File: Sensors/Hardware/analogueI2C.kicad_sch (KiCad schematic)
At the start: 136 parts, among them J10 1053131104, J11 1053131104, J12 1053131104, J13 1053131104, J14 1053131104, J3 1053131104, J4 1053131104, J5 1053131104, J6 1053131104, J7 1053131104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

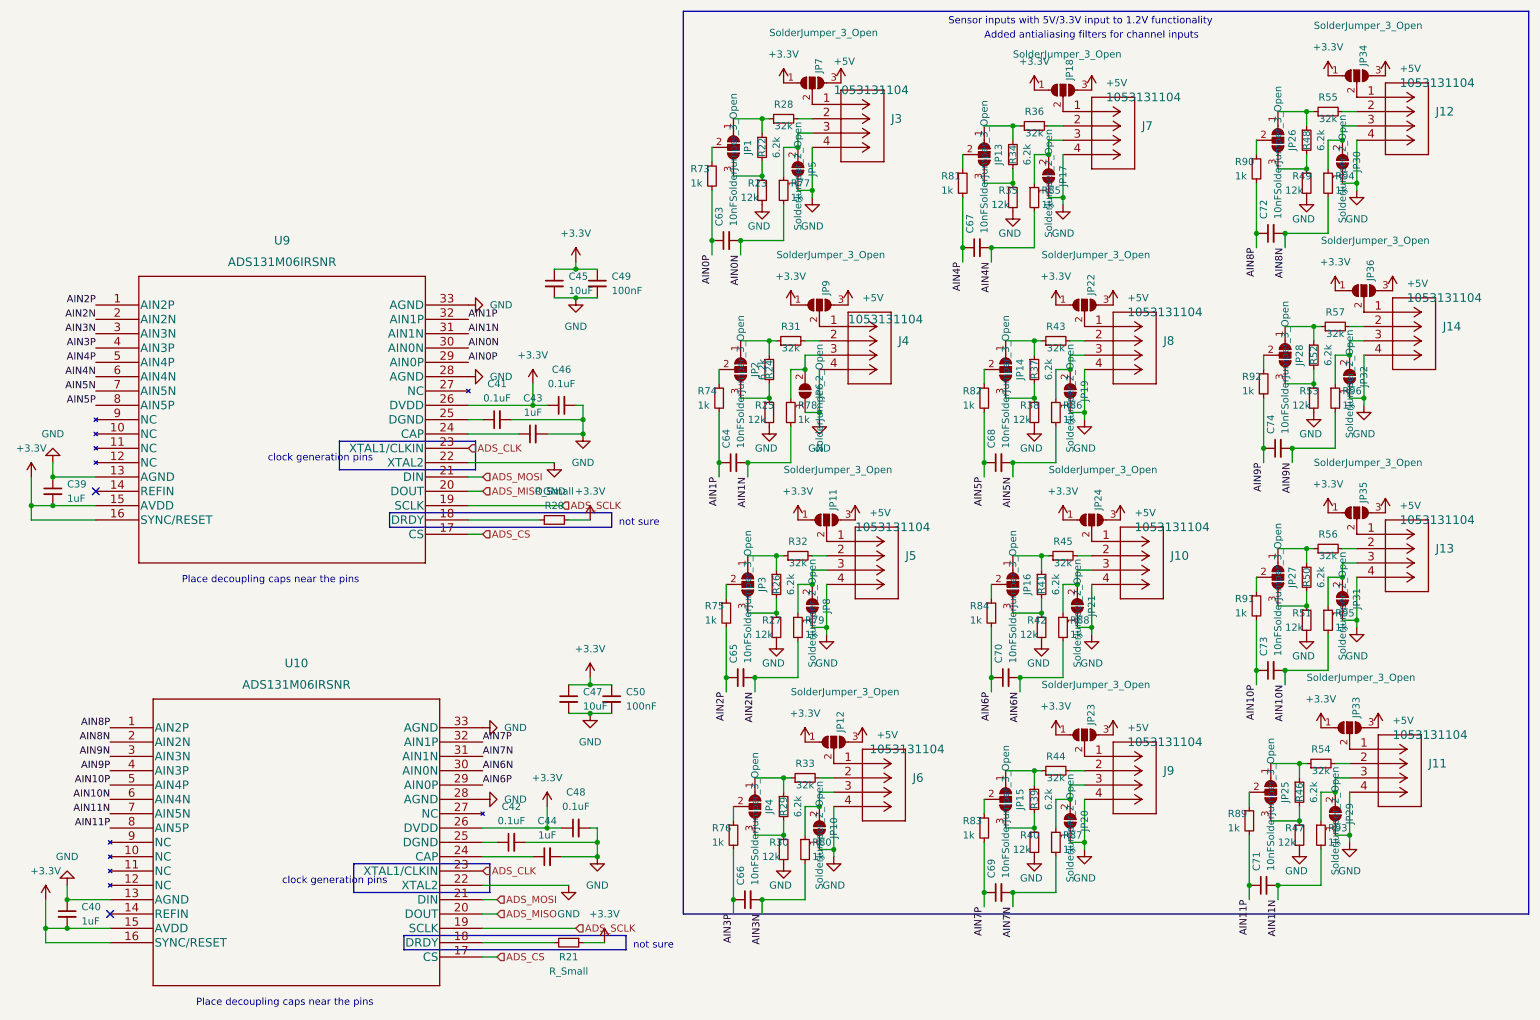
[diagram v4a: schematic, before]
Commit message: ADC connections and KiCAD version update
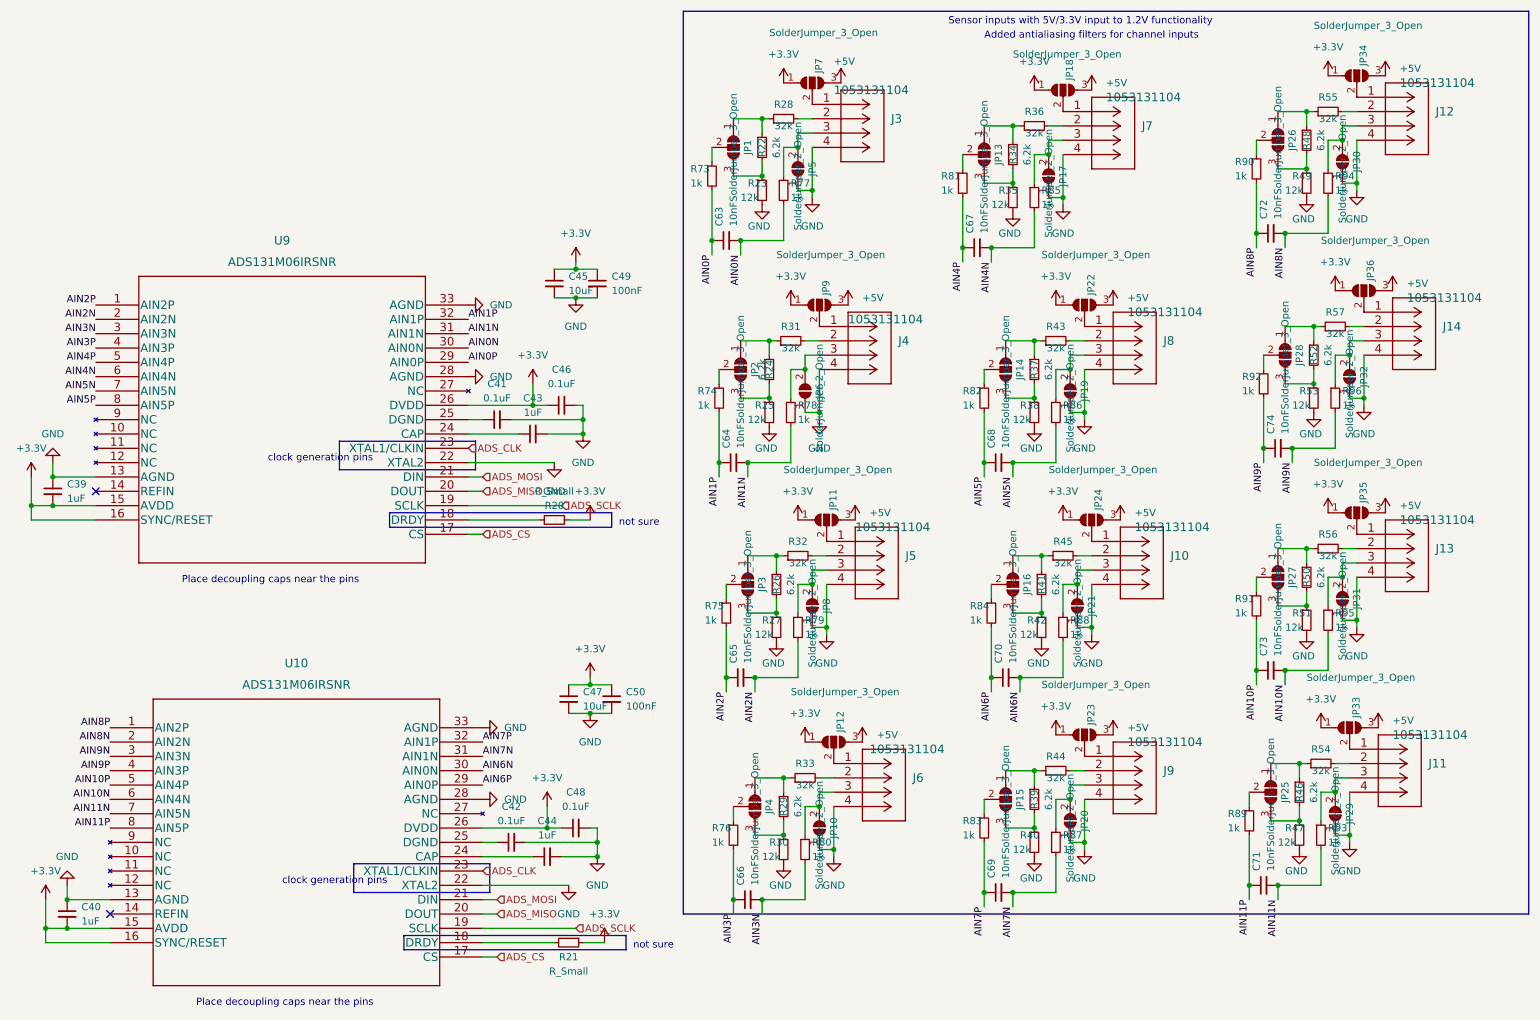
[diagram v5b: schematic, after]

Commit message: spacings and redo lines with tps
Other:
- note added: "10V option"
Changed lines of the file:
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@@
+    (effects (font (size 1.27 1.27)) (justify left bottom))
+  )
+  (text "10V option" (at 165.1 81.28 0)
     (effects (font (size 1.27 1.27)) (justify left bottom))
   )
@@
     (effects (font (size 1.27 1.27)) (justify left bottom))
   )
+  (text "10V option" (at 212.09 157.48 0)
+    (effects (font (size 1.27 1.27)) (justify left bottom))
+  )

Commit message: changed pins layout for esp
update for ADC traces
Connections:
- net +5V: no longer JP33.3 (B), JP35.3 (B)
- new net +10V: JP33.3 (B), JP35.3 (B)
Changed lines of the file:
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@@
     (effects (font (size 1.27 1.27)) (justify left bottom))
   )
-  (text "10V option" (at 165.1 81.28 0)
+  (text "10V option" (at 259.08 118.11 0)
     (effects (font (size 1.27 1.27)) (justify left bottom))
   )
@@
     (effects (font (size 1.27 1.27)) (justify left bottom))
   )
-  (text "10V option" (at 212.09 157.48 0)
+  (text "10V option" (at 257.81 157.48 0)
     (effects (font (size 1.27 1.27)) (justify left bottom))
   )
@@
     )
   )
-  (symbol (lib_id "power:+5V") (at 259.08 101.6 0) (unit 1)
-    (in_bom yes) (on_board yes) (dnp no) (fields_autoplaced)
-    (property "Reference" "#PWR0128" (at 259.08 105.41 0)
-      (effects (font (size 1.27 1.27)) hide)
-    )
-    (property "Value" "+5V" (at 261.62 100.3299 0)
-      (effects (font (size 1.27 1.27)) (justify left))
-    )
-    (property "Footprint" "" (at 259.08 101.6 0)
-      (effects (font (size 1.27 1.27)) hide)
-    )
-    (property "Datasheet" "" (at 259.08 101.6 0)
-      (effects (font (size 1.27 1.27)) hide)
-    )
-    (pin "1")
-    (instances
-      (project "sensorboard"
-        (path "/26801cfb-b53b-4a6a-a2f4-5f4986565765/00000000-0000-0000-0000-000061b9f0c0"
-          (reference "#PWR0128") (unit 1)
-        )
-      )
-    )
-  )
   (symbol (lib_id "Device:R_Small") (at 243.84 158.75 0) (unit 1)
     (in_bom yes) (on_board yes) (dnp no)
@@
     )
   )
+  (symbol (lib_id "power:+10V") (at 257.81 139.7 0) (unit 1)
+    (in_bom yes) (on_board yes) (dnp no) (fields_autoplaced)
+    (property "Reference" "#PWR023" (at 257.81 143.51 0)
+      (effects (font (size 1.27 1.27)) hide)
+    )
+    (property "Value" "+10V" (at 257.81 135.89 0)
+      (effects (font (size 1.27 1.27)))
+    )
+    (property "Footprint" "" (at 257.81 139.7 0)
+      (effects (font (size 1.27 1.27)) hide)
+    )
+    (property "Datasheet" "" (at 257.81 139.7 0)
+      (effects (font (size 1.27 1.27)) hide)
+    )
+    (pin "1")
+    (instances
+      (project "sensorboard"
+        (path "/26801cfb-b53b-4a6a-a2f4-5f4986565765/00000000-0000-0000-0000-000061b9f0c0"
+          (reference "#PWR023") (unit 1)
+        )
+      )
+    )
+  )
   (symbol (lib_id "Device:R_Small") (at 248.92 43.18 0) (unit 1)
     (in_bom yes) (on_board yes) (dnp no)
@@
     )
   )
+  (symbol (lib_id "power:+10V") (at 259.08 101.6 0) (unit 1)
+    (in_bom yes) (on_board yes) (dnp no) (fields_autoplaced)
+    (property "Reference" "#PWR022" (at 259.08 105.41 0)
+      (effects (font (size 1.27 1.27)) hide)
+    )
+    (property "Value" "+10V" (at 259.08 97.79 0)
+      (effects (font (size 1.27 1.27)))
+    )
+    (property "Footprint" "" (at 259.08 101.6 0)
+      (effects (font (size 1.27 1.27)) hide)
+    )
+    (property "Datasheet" "" (at 259.08 101.6 0)
+      (effects (font (size 1.27 1.27)) hide)
+    )
+    (pin "1")
+    (instances
+      (project "sensorboard"
+        (path "/26801cfb-b53b-4a6a-a2f4-5f4986565765/00000000-0000-0000-0000-000061b9f0c0"
+          (reference "#PWR022") (unit 1)
+        )
+      )
+    )
+  )
   (symbol (lib_id "Jumper:SolderJumper_3_Open") (at 207.01 102.87 0) (unit 1)
     (in_bom yes) (on_board yes) (dnp no)
@@
         )
       )
-    )
-  )
-  (symbol (lib_id "power:+5V") (at 257.81 139.7 0) (unit 1)
-    (in_bom yes) (on_board yes) (dnp no) (fields_autoplaced)
-    (property "Reference" "#PWR0126" (at 257.81 143.51 0)
-      (effects (font (size 1.27 1.27)) hide)
-    )
-    (property "Value" "+5V" (at 260.35 138.4299 0)
-      (effects (font (size 1.27 1.27)) (justify left))
-    )
-    (property "Footprint" "" (at 257.81 139.7 0)
-      (effects (font (size 1.27 1.27)) hide)
-    )
-    (property "Datasheet" "" (at 257.81 139.7 0)
-      (effects (font (size 1.27 1.27)) hide)
-    )
-    (pin "1")
-    (instances
-      (project "sensorboard"
-        (path "/26801cfb-b53b-4a6a-a2f4-5f4986565765/00000000-0000-0000-0000-000061b9f0c0"
-          (reference "#PWR0126") (unit 1)
-        )
-      )

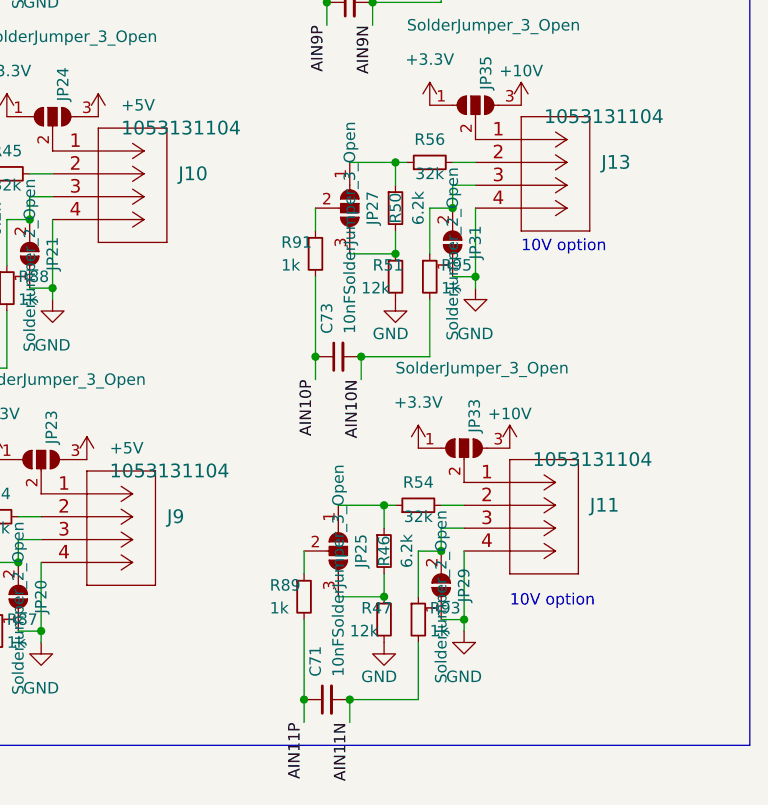
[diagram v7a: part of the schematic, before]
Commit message: added values for the 10V option
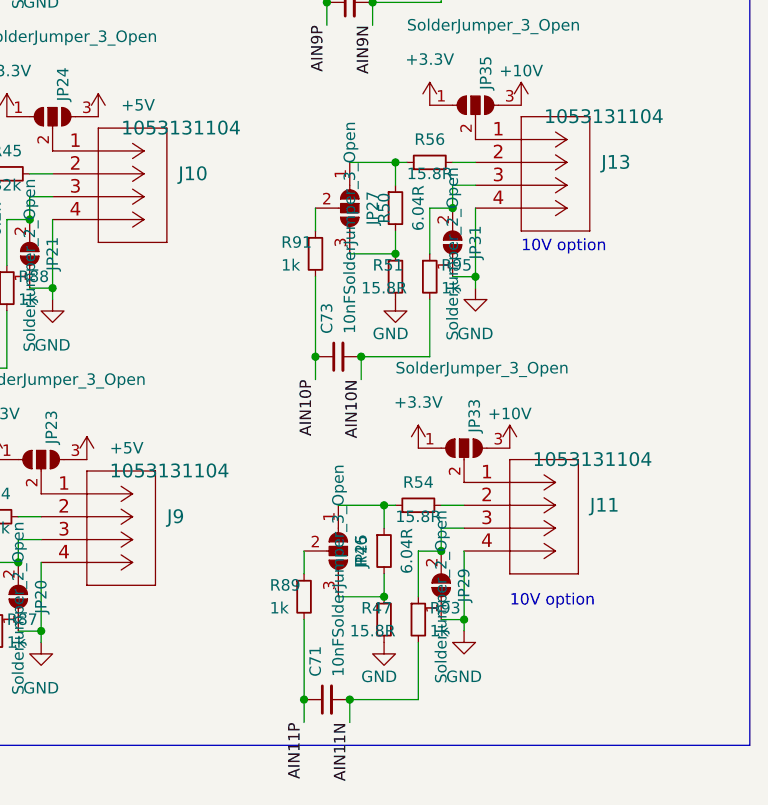
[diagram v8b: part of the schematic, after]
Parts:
- R46, R50: value 6.2k -> 6.04R
- R47, R51: value 12k -> 15.8R
- R54, R56: value 32k -> 15.8R
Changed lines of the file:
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@@
       (effects (font (size 1.27 1.27)) (justify left))
     )
-    (property "Value" "12k" (at 240.03 160.02 0)
+    (property "Value" "15.8R" (at 240.03 160.02 0)
       (effects (font (size 1.27 1.27)) (justify left))
     )
@@
       (effects (font (size 1.27 1.27)))
     )
-    (property "Value" "32k" (at 247.65 147.32 90)
+    (property "Value" "15.8R" (at 247.65 147.32 90)
       (effects (font (size 1.27 1.27)))
     )
@@
       (effects (font (size 1.27 1.27)))
     )
-    (property "Value" "32k" (at 248.92 109.22 90)
+    (property "Value" "15.8R" (at 248.92 109.22 90)
       (effects (font (size 1.27 1.27)))
     )
@@
       (effects (font (size 1.27 1.27)) (justify left))
     )
-    (property "Value" "12k" (at 241.3 121.92 0)
+    (property "Value" "15.8R" (at 241.3 121.92 0)
       (effects (font (size 1.27 1.27)) (justify left))
     )
@@
   (symbol (lib_id "Device:R_Small") (at 243.84 151.13 0) (unit 1)
     (in_bom yes) (on_board yes) (dnp no)
-    (property "Reference" "R46" (at 243.84 151.13 90)
+    (property "Reference" "R46" (at 241.3 151.13 90)
       (effects (font (size 1.27 1.27)))
     )
-    (property "Value" "6.2k" (at 246.38 151.13 90)
+    (property "Value" "6.04R" (at 246.38 151.13 90)
       (effects (font (size 1.27 1.27)))
     )
@@
   (symbol (lib_id "Device:R_Small") (at 245.11 113.03 0) (unit 1)
     (in_bom yes) (on_board yes) (dnp no)
-    (property "Reference" "R50" (at 245.11 113.03 90)
+    (property "Reference" "R50" (at 243.84 113.03 90)
       (effects (font (size 1.27 1.27)))
     )
-    (property "Value" "6.2k" (at 247.65 113.03 90)
+    (property "Value" "6.04R" (at 247.65 113.03 90)
       (effects (font (size 1.27 1.27)))
     )
